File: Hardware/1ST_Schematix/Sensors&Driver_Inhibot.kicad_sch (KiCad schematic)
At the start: 13 parts, among them U401 LSM6DSL, U402 DRV8833PW

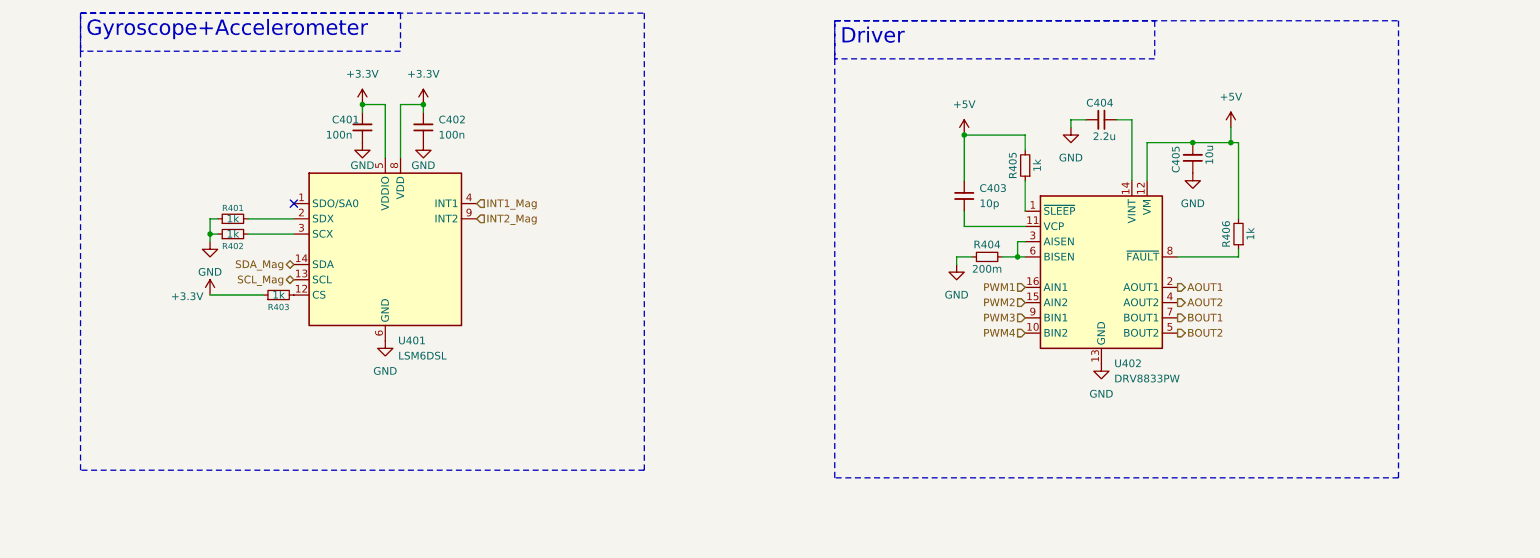
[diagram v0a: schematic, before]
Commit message: Update KiCad and STM32CubeMX
Ready for the check-in
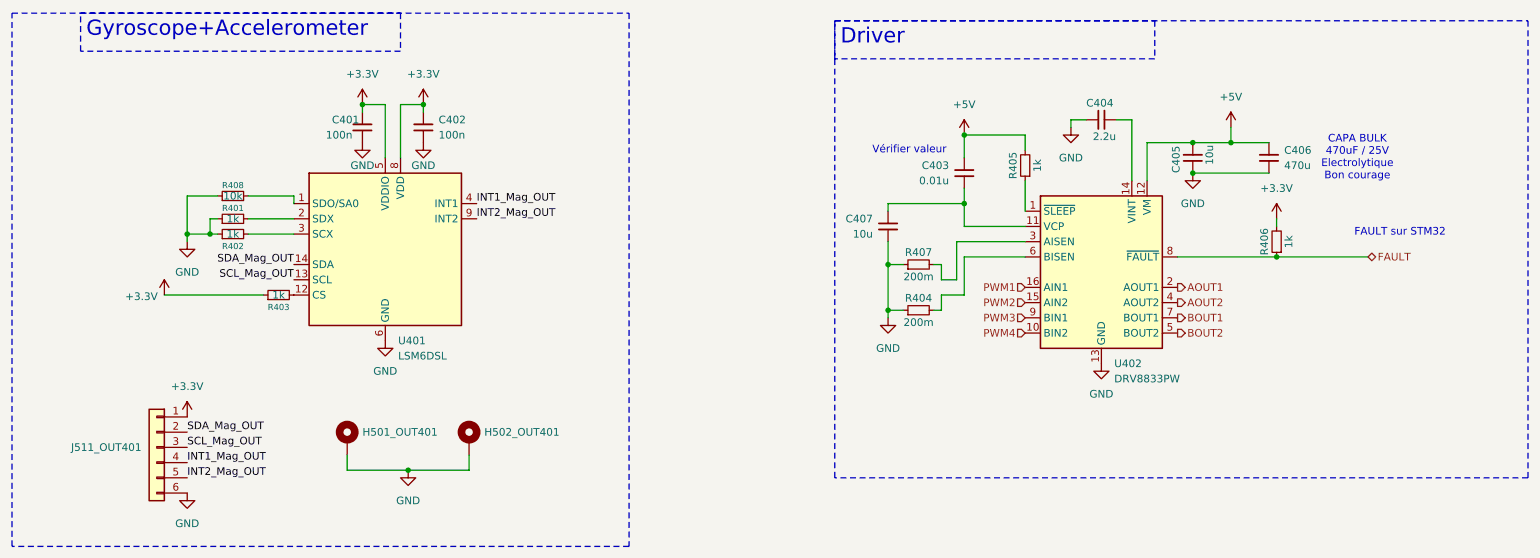
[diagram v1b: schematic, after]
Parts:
- added C406: 470u, Capacitor_THT:CP_Radial_Tantal_D8.0mm_P2.50mm, symbol Device:C_Small
- added C407: 10u, Capacitor_SMD:C_0402_1005Metric, symbol Device:C_Small
- added H501_OUT401, H502_OUT401: MountingHole_Pad, Module:Maple_Mini, symbol Mechanical:MountingHole_Pad
- added J511_OUT401: Conn_01x06, symbol Connector_Generic:Conn_01x06
- added R407: 200m, Resistor_THT:R_Array_SIP4, symbol Device:R_Small
- added R408: 10k, Resistor_SMD:R_0402_1005Metric, symbol Device:R_Small
- C403: value 10p -> 0.01u
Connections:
- net +3.3V: now also R406.2, J511_OUT401.1 (Pin_1)
- net +5V: now also C406.1; no longer R406.2
- net GND: now also C406.2, C407.1, H501_OUT401.1, H502_OUT401.1, J511_OUT401.6 (Pin_6), R407.1, R408.1
- net at U401.1 (SDO/SA0): now also R408.2
- net at C403.1, U402.11 (VCP): now also C407.2
- net FAULT: now reaches R406.1, U402.8 (~{FAULT})
- net at R404.2, U402.6 (BISEN): no longer U402.3 (AISEN)
- net INT1_Mag renamed INT1_Mag_OUT
- net INT1_Mag_OUT: now also J511_OUT401.4 (Pin_4)
- net INT2_Mag renamed INT2_Mag_OUT
- net INT2_Mag_OUT: now also J511_OUT401.5 (Pin_5)
- net SCL_Mag renamed SCL_Mag_OUT
- net SCL_Mag_OUT: now also J511_OUT401.3 (Pin_3)
- net SDA_Mag renamed SDA_Mag_OUT
- net SDA_Mag_OUT: now also J511_OUT401.2 (Pin_2)
- new net: R407.2, U402.3 (AISEN)
- no-connect marks 1 -> 0
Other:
- note added: "CAPA BULK 470uF / 25V Electrolytique Bon courage"
- note added: "FAULT sur STM32"
- note added: "Vérifier valeur"
- moved on the sheet: C403, R404

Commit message: schematic review with esteemed professor
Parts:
- removed C406: 470u, Capacitor_THT:CP_Radial_Tantal_D8.0mm_P2.50mm, symbol Device:C_Small
- removed C407: 10u, Capacitor_SMD:C_0402_1005Metric, symbol Device:C_Small
- added C406: 470u, Capacitor_SMD:CP_Elec_10x10.5, symbol Device:C_Polarized_Small
- C401, C402: JLCPCB Part # (none) -> C1525
- C403: value 0.01u -> 10n
- R404, R407: footprint Resistor_THT:R_Array_SIP4 -> (none)
- R405, R406: footprint Resistor_THT:R_Array_SIP4 -> Resistor_SMD:R_0402_1005Metric
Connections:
- net +5V: now also C406.1
- net GND: now also C406.2
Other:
- note removed: "CAPA BULK 470uF / 25V Electrolytique Bon courage"
- note removed: "Vérifier valeur"
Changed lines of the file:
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@@
 		)
 	)
-	(text "Vérifier valeur"
-		(exclude_from_sim no)
-		(at 176.276 78.74 0)
-		(effects
-			(font
-				(size 1.27 1.27)
-				(color 255 0 0 1)
-			)
-		)
-	)
 	(text "FAULT sur STM32"
 		(exclude_from_sim no)
@@
 		)
 	)
-	(text "CAPA BULK\n470uF / 25V\nElectrolytique\nBon courage"
-		(exclude_from_sim no)
-		(at 250.952 80.01 0)
-		(effects
-			(font
-				(size 1.27 1.27)
-			)
-		)
-	)
 	(text_box "Driver"
 		(exclude_from_sim no)
@@
 	)
 	(junction
-		(at 172.72 97.79)
-		(diameter 0)
-		(color 0 0 0 0)
-	)
-	(junction
 		(at 85.09 71.12)
 		(diameter 0)
@@
 	)
 	(junction
-		(at 185.42 87.63)
-		(diameter 0)
-		(color 0 0 0 0)
-	)
-	(junction
 		(at 55.88 92.71)
 		(diameter 0)
@@
 	(wire
 		(pts
-			(xy 172.72 87.63) (xy 185.42 87.63)
-		)
-		(stroke
-			(width 0)
-			(type default)
-		)
-	)
-	(wire
-		(pts
 			(xy 252.73 96.52) (xy 237.49 96.52)
 		)
@@
 	(wire
 		(pts
-			(xy 172.72 93.98) (xy 172.72 97.79)
-		)
-		(stroke
-			(width 0)
-			(type default)
-		)
-	)
-	(wire
-		(pts
 			(xy 88.9 80.01) (xy 88.9 71.12)
 		)
@@
 	(wire
 		(pts
-			(xy 172.72 87.63) (xy 172.72 88.9)
-		)
-		(stroke
-			(width 0)
-			(type default)
-		)
-	)
-	(wire
-		(pts
 			(xy 175.26 97.79) (xy 172.72 97.79)
 		)
@@
 			)
 		)
-		(property "Footprint" "Resistor_THT:R_Array_SIP4"
+		(property "Footprint" ""
 			(at 177.8 97.79 0)
 			(hide yes)
@@
 			)
 		)
-		(property "Footprint" "Resistor_THT:R_Array_SIP4"
+		(property "Footprint" "Resistor_SMD:R_0402_1005Metric"
 			(at 237.49 93.98 0)
 			(hide yes)
@@
 	)
 	(symbol
-		(lib_id "Device:C_Small")
-		(at 172.72 91.44 0)
-		(mirror x)
-		(unit 1)
-		(body_style 1)
-		(exclude_from_sim no)
-		(in_bom yes)
-		(on_board yes)
-		(in_pos_files yes)
-		(dnp no)
-		(property "Reference" "C407"
-			(at 170.18 90.1699 0)
-			(show_name no)
-			(do_not_autoplace no)
-			(effects
-				(font
-					(size 1.27 1.27)
-				)
-				(justify right)
-			)
-		)
-		(property "Value" "10u"
-			(at 170.18 92.7099 0)
-			(show_name no)
-			(do_not_autoplace no)
-			(effects
-				(font
-					(size 1.27 1.27)
-				)
-				(justify right)
-			)
-		)
-		(property "Footprint" "Capacitor_SMD:C_0402_1005Metric"
-			(at 172.72 91.44 0)
-			(hide yes)
-			(show_name no)
-			(do_not_autoplace no)
-			(effects
-				(font
-					(size 1.27 1.27)
-				)
-			)
-		)
-		(property "Datasheet" ""
-			(at 172.72 91.44 0)
-			(hide yes)
-			(show_name no)
-			(do_not_autoplace no)
-			(effects
-				(font
-					(size 1.27 1.27)
-				)
-			)
-		)
-		(property "Description" "Unpolarized capacitor, small symbol"
-			(at 172.72 81.28 0)
-			(hide yes)
-			(show_name no)
-			(do_not_autoplace no)
-			(effects
-				(font
-					(size 1.27 1.27)
-				)
-			)
-		)
-		(pin "1"
-		)
-		(pin "2"
-		)
-		(instances
-			(project "1ST_Schematix"
-				(path "/59c2502d-7c28-4023-9b54-15ec9e15e6d4/bf29c48a-0938-4b44-b61a-f77bea55e593"
-					(reference "C407")
-					(unit 1)
-				)
-			)
-		)
-	)
-	(symbol
 		(lib_id "Device:R_Small")
 		(at 63.5 90.17 90)
@@
 			)
 		)
-		(property "Value" "0.01u"
+		(property "Value" "10n"
 			(at 182.88 83.8199 0)
 			(show_name no)
@@
 	)
 	(symbol
+		(lib_id "Device:C_Polarized_Small")
+		(at 236.22 80.01 0)
+		(unit 1)
+		(body_style 1)
+		(exclude_from_sim no)
+		(in_bom yes)
+		(on_board yes)
+		(in_pos_files yes)
+		(dnp no)
+		(fields_autoplaced yes)
+		(property "Reference" "C406"
+			(at 238.76 78.1938 0)
+			(show_name no)
+			(do_not_autoplace no)
+			(effects
+				(font
+					(size 1.27 1.27)
+				)
+				(justify left)
+			)
+		)
+		(property "Value" "470u"
+			(at 238.76 80.7338 0)
+			(show_name no)
+			(do_not_autoplace no)
+			(effects
+				(font
+					(size 1.27 1.27)
+				)
+				(justify left)
+			)
+		)
+		(property "Footprint" "Capacitor_SMD:CP_Elec_10x10.5"
+			(at 236.22 80.01 0)
+			(hide yes)
+			(show_name no)
+			(do_not_autoplace no)
+			(effects
+				(font
+					(size 1.27 1.27)
+				)
+			)
+		)
+		(property "Datasheet" ""
+			(at 236.22 80.01 0)
+			(hide yes)
+			(show_name no)
+			(do_not_autoplace no)
+			(effects
+				(font
+					(size 1.27 1.27)
+				)
+			)
+		)
+		(property "Description" "Polarized capacitor, small symbol"
+			(at 236.22 80.01 0)
+			(hide yes)
+			(show_name no)
+			(do_not_autoplace no)
+			(effects
+				(font
+					(size 1.27 1.27)
+				)
+			)
+		)
+		(property "JLCPCB Part #" "C178566"
+			(at 236.22 80.01 0)
+			(hide yes)
+			(show_name no)
+			(do_not_autoplace no)
+			(effects
+				(font
+					(size 1.27 1.27)
+				)
+			)
+		)
+		(pin "1"
+		)
+		(pin "2"
+		)
+		(instances
+			(project "1ST_Schematix"
+				(path "/59c2502d-7c28-4023-9b54-15ec9e15e6d4/bf29c48a-0938-4b44-b61a-f77bea55e593"
+					(reference "C406")
+					(unit 1)
+				)
+			)
+		)
+	)
+	(symbol
 		(lib_id "power:GND")
 		(at 208.28 114.3 0)
@@
 			)
 		)
-		(property "Footprint" "Resistor_THT:R_Array_SIP4"
+		(property "Footprint" "Resistor_SMD:R_0402_1005Metric"
 			(at 195.58 81.28 0)
 			(hide yes)
@@
 			)
 		)
-		(pin "1"
-		)
-		(pin "2"
-		)
-		(instances
-			(project "1ST_Schematix"
-				(path "/59c2502d-7c28-4023-9b54-15ec9e15e6d4/bf29c48a-0938-4b44-b61a-f77bea55e593"
-					(reference "C402")
-					(unit 1)
-				)
-			)
-		)
-	)
-	(symbol
-		(lib_id "Device:C_Small")
-		(at 236.22 80.01 0)
-		(unit 1)
-		(body_style 1)
-		(exclude_from_sim no)
-		(in_bom yes)
-		(on_board yes)
-		(in_pos_files yes)
-		(dnp no)
-		(fields_autoplaced yes)
-		(property "Reference" "C406"
-			(at 238.76 78.7399 0)
-			(show_name no)
-			(do_not_autoplace no)
-			(effects
-				(font
-					(size 1.27 1.27)
-				)
-				(justify left)
-			)
-		)
-		(property "Value" "470u"
-			(at 238.76 81.2799 0)
-			(show_name no)
-			(do_not_autoplace no)
-			(effects
-				(font
-					(size 1.27 1.27)
-				)
-				(justify left)
-			)
-		)
-		(property "Footprint" "Capacitor_THT:CP_Radial_Tantal_D8.0mm_P2.50mm"
-			(at 236.22 80.01 0)
-			(hide yes)
-			(show_name no)
-			(do_not_autoplace no)
-			(effects
-				(font
-					(size 1.27 1.27)
-				)
-			)
-		)
-		(property "Datasheet" ""
-			(at 236.22 80.01 0)
-			(hide yes)
-			(show_name no)
-			(do_not_autoplace no)
-			(effects
-				(font
-					(size 1.27 1.27)
-				)
-			)
-		)
-		(property "Description" "Unpolarized capacitor, small symbol"
-			(at 236.22 90.17 0)
+		(property "JLCPCB Part #" "C1525"
+			(at 95.25 74.93 0)
 			(hide yes)
 			(show_name no)
@@
 			)
 		)
-		(property "JLCPCB Part #" "C9900016268"
-			(at 236.22 80.01 0)
-			(hide yes)
-			(show_name no)
-			(do_not_autoplace no)
-			(effects
-				(font
-					(size 1.27 1.27)
-				)
-			)
+		(pin "1"
 		)
 		(pin "2"
 		)
-		(pin "1"
-		)
 		(instances
 			(project "1ST_Schematix"
 				(path "/59c2502d-7c28-4023-9b54-15ec9e15e6d4/bf29c48a-0938-4b44-b61a-f77bea55e593"
-					(reference "C406")
+					(reference "C402")
 					(unit 1)
 				)
@@
 			)
 		)
-		(property "Footprint" "Resistor_THT:R_Array_SIP4"
+		(property "Footprint" ""
 			(at 177.8 105.41 0)
 			(hide yes)
@@
 			(hide yes)
 			(show_name no)
+			(do_not_autoplace no)
+			(effects
+				(font
+					(size 1.27 1.27)
+				)
+			)
+		)
+		(property "JLCPCB Part #" "C1525"
+			(at 85.09 74.93 0)
+			(hide yes)
+			(show_name no)

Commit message: prints for component except 10mOhm
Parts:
- H501_OUT401, H502_OUT401: footprint Module:Maple_Mini -> MountingHole:MountingHole_3.2mm_M3_ISO14580_Pad
- J511_OUT401: footprint (none) -> Connector_JST:JST_EH_B6B-EH-A_1x06_P2.50mm_Vertical; now left out of the parts list
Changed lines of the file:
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@@
 			)
 		)
-		(property "Footprint" "Module:Maple_Mini"
+		(property "Footprint" "MountingHole:MountingHole_3.2mm_M3_ISO14580_Pad"
 			(at 82.55 127 0)
 			(hide yes)
@@
 			)
 		)
-		(property "Footprint" "Module:Maple_Mini"
+		(property "Footprint" "MountingHole:MountingHole_3.2mm_M3_ISO14580_Pad"
 			(at 102.87 127 0)
 			(hide yes)
@@
 		(body_style 1)
 		(exclude_from_sim no)
-		(in_bom yes)
+		(in_bom no)
 		(on_board yes)
 		(in_pos_files yes)
@@
 			)
 		)
-		(property "Footprint" ""
+		(property "Footprint" "Connector_JST:JST_EH_B6B-EH-A_1x06_P2.50mm_Vertical"
 			(at 50.8 128.27 0)
 			(hide yes)

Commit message: all footprints done
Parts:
- R404, R407: footprint (none) -> Resistor_SMD:R_0805_2012Metric; JLCPCB Part # (none) -> C2074761
